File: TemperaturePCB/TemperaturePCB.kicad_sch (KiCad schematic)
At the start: 3 parts, among them J1 Conn_01x02_Socket

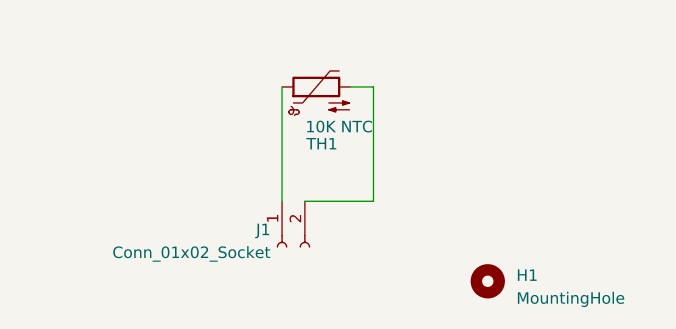
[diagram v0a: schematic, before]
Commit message: Updated temperature sensor PCB board
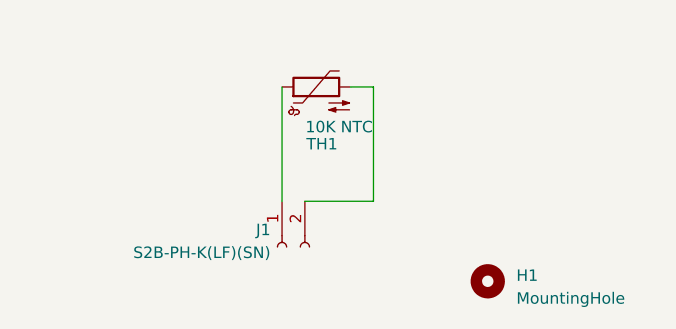
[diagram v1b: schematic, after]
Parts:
- H1: footprint MountingHole:MountingHole_6.4mm_M6_Pad_Via -> MountingHole:MountingHole_6.5mm_Pad_Via
- J1: value Conn_01x02_Socket -> S2B-PH-K(LF)(SN); footprint Connector_PinSocket_2.54mm:PinSocket_1x02_P2.54mm_Vertical -> Connector_JST:JST_PH_S2B-PH-K_1x02_P2.00mm_Horizontal; LCSCStockCode (none) -> C265016
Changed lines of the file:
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@@
       (effects (font (size 1.27 1.27)) (justify left))
     )
-    (property "Footprint" "MountingHole:MountingHole_6.4mm_M6_Pad_Via" (at 146.05 96.52 0)
+    (property "Footprint" "MountingHole:MountingHole_6.5mm_Pad_Via" (at 146.05 96.52 0)
       (effects (font (size 1.27 1.27)) hide)
     )
@@
       (effects (font (size 1.27 1.27)) (justify left))
     )
-    (property "Value" "Conn_01x02_Socket" (at 121.92 93.345 90)
+    (property "Value" "S2B-PH-K(LF)(SN)" (at 121.92 93.345 90)
       (effects (font (size 1.27 1.27)) (justify left))
     )
-    (property "Footprint" "Connector_PinSocket_2.54mm:PinSocket_1x02_P2.54mm_Vertical" (at 123.19 92.71 0)
+    (property "Footprint" "Connector_JST:JST_PH_S2B-PH-K_1x02_P2.00mm_Horizontal" (at 123.19 92.71 0)
       (effects (font (size 1.27 1.27)) hide)
     )
@@
       (effects (font (size 1.27 1.27)) hide)
     )
+    (property "LCSCStockCode" "C265016" (at 123.19 92.71 90)
+      (effects (font (size 1.27 1.27)) hide)
+    )

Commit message: Swap JST_PH_S2B-PH-K_1x02 to SMD PH-SM4-TB
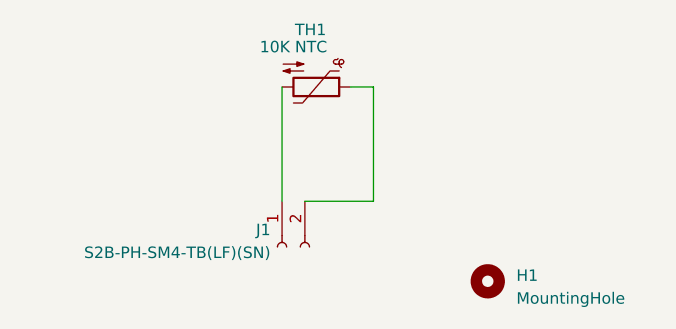
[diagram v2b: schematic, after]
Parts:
- J1: value S2B-PH-K(LF)(SN) -> S2B-PH-SM4-TB(LF)(SN); footprint Connector_JST:JST_PH_S2B-PH-K_1x02_P2.00mm_Horizontal -> Connector_JST:JST_PH_S2B-PH-SM4-TB_1x02-1MP_P2.00mm_Horizontal; LCSCStockCode C265016 -> C295747
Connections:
- net at J1.1 (Pin_1): now also TH1.2; no longer TH1.1
- net at J1.2 (Pin_2): now also TH1.1; no longer TH1.2
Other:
- moved on the sheet: TH1
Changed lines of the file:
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@@
       (effects (font (size 1.27 1.27)) (justify left))
     )
-    (property "Value" "S2B-PH-K(LF)(SN)" (at 121.92 93.345 90)
+    (property "Value" "S2B-PH-SM4-TB(LF)(SN)" (at 121.92 93.345 90)
       (effects (font (size 1.27 1.27)) (justify left))
     )
-    (property "Footprint" "Connector_JST:JST_PH_S2B-PH-K_1x02_P2.00mm_Horizontal" (at 123.19 92.71 0)
+    (property "Footprint" "Connector_JST:JST_PH_S2B-PH-SM4-TB_1x02-1MP_P2.00mm_Horizontal" (at 123.19 92.71 0)
       (effects (font (size 1.27 1.27)) hide)
     )
@@
       (effects (font (size 1.27 1.27)) hide)
     )
-    (property "LCSCStockCode" "C265016" (at 123.19 92.71 90)
+    (property "LCSCStockCode" "C295747" (at 123.19 92.71 90)
       (effects (font (size 1.27 1.27)) hide)
     )
@@
     )
   )
-  (symbol (lib_id "Device:Thermistor_NTC") (at 127 74.93 90) (unit 1)
+  (symbol (lib_id "Device:Thermistor_NTC") (at 127 74.93 270) (unit 1)
     (in_bom yes) (on_board yes) (dnp no)
-    (property "Reference" "TH1" (at 127.635 81.28 90)
+    (property "Reference" "TH1" (at 126.365 68.58 90)
       (effects (font (size 1.27 1.27)))
     )
-    (property "Value" "10K NTC" (at 129.54 79.375 90)
+    (property "Value" "10K NTC" (at 124.46 70.485 90)
       (effects (font (size 1.27 1.27)))
     )
-    (property "Footprint" "Resistor_SMD:R_0805_2012Metric" (at 125.73 74.93 0)
+    (property "Footprint" "Resistor_SMD:R_0805_2012Metric" (at 128.27 74.93 0)
       (effects (font (size 1.27 1.27)) hide)
     )
-    (property "Datasheet" "https://datasheet.lcsc.com/szlcsc/Guangdong-Fenghua-Advanced-Tech-CMFB103F3950FANT_C51597.pdf" (at 125.73 74.93 0)
+    (property "Datasheet" "https://datasheet.lcsc.com/szlcsc/Guangdong-Fenghua-Advanced-Tech-CMFB103F3950FANT_C51597.pdf" (at 128.27 74.93 0)
       (effects (font (size 1.27 1.27)) hide)
     )
